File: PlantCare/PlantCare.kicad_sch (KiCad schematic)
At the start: 5 parts, among them U1 AMS1117-3.3

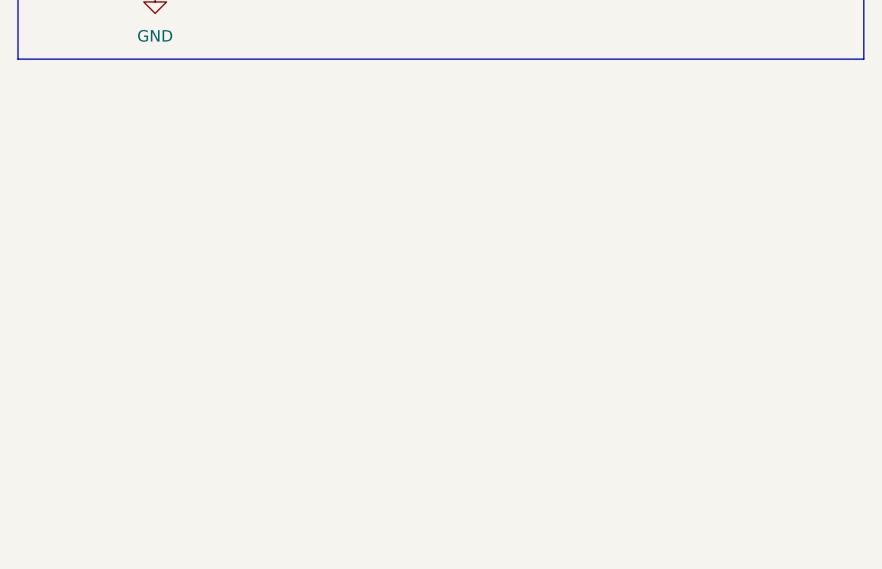
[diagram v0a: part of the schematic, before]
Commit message: Add micro usb scheme
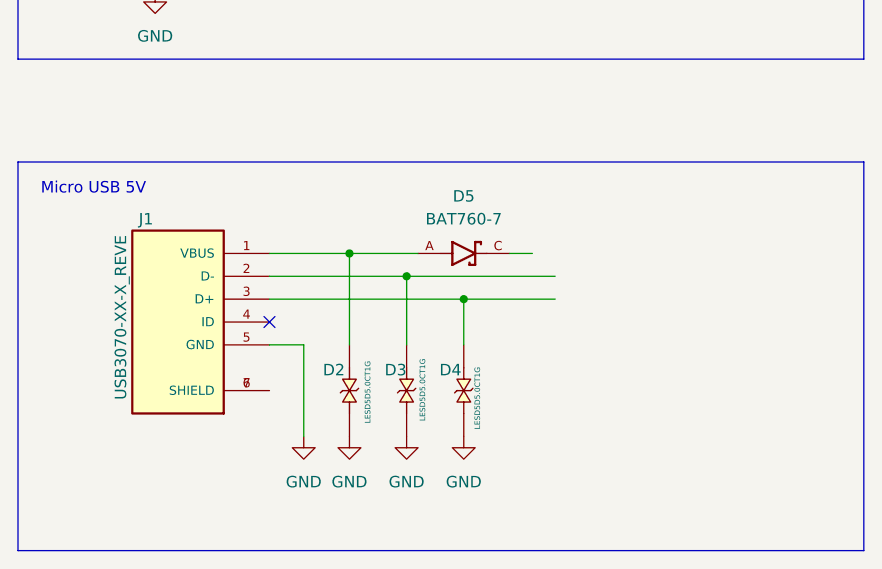
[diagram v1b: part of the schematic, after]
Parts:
- added D2, D3, D4: LESD5D5.0CT1G, TVS_LESD5D5.0CT1G, symbol LESD5D5.0CT1G:LESD5D5.0CT1G
- added D5: BAT760-7, BAT760-7:SOD2513X120N, symbol BAT760-7:BAT760-7
- added J1: USB3070-XX-X_REVE, USB3070-XX-X_REVE:GCT_USB3070-XX-X_REVE, symbol USB3070-XX-X_REVE:USB3070-XX-X_REVE
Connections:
- net GND: now also D2.1, D3.1, D4.2, J1.5 (GND)
- new net: D2.2, D5.A, J1.1 (VBUS)
- new net: D3.2, J1.2 (D-)
- new net: D4.1, J1.3 (D+)
- new net: J1.6 (SHIELD), J1.7 (SHIELD)
- no-connect marks 0 -> 1
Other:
- note added: "Micro USB 5V"

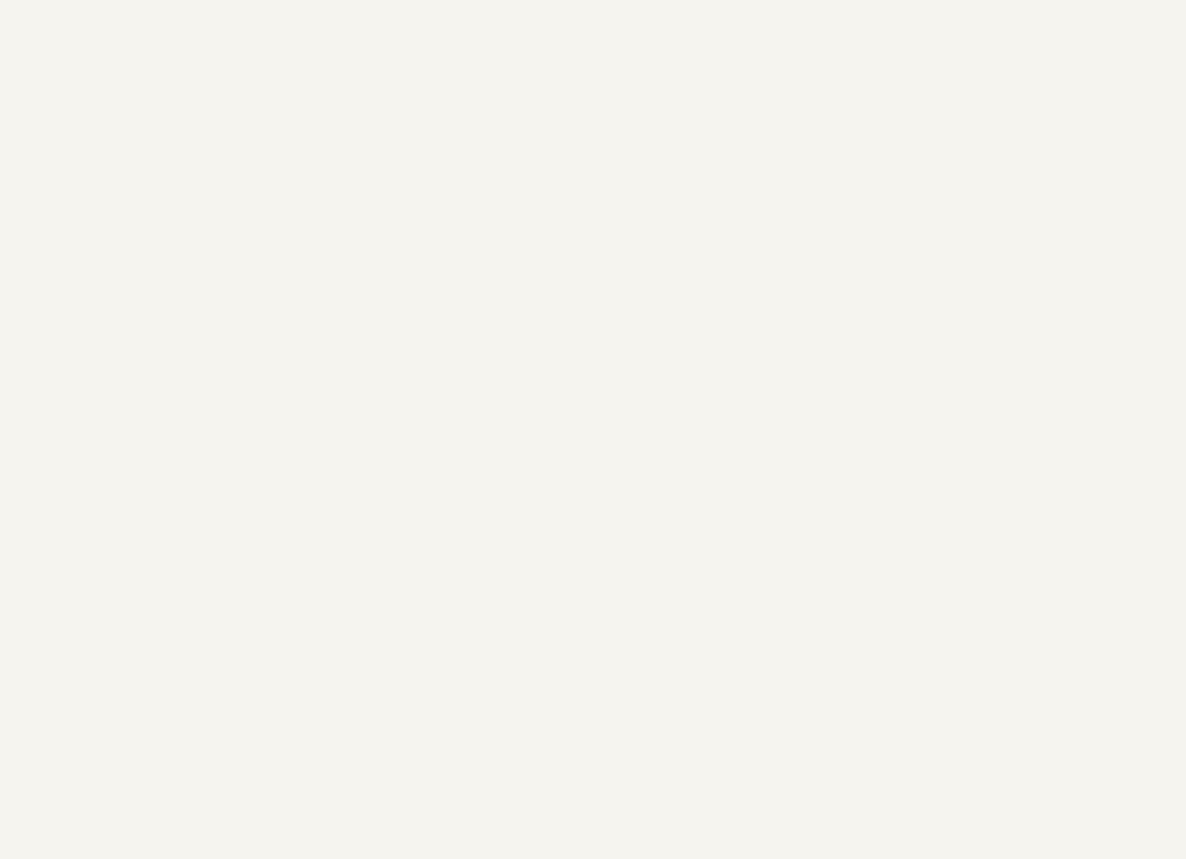
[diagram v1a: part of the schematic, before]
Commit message: Add esp32 module scheme
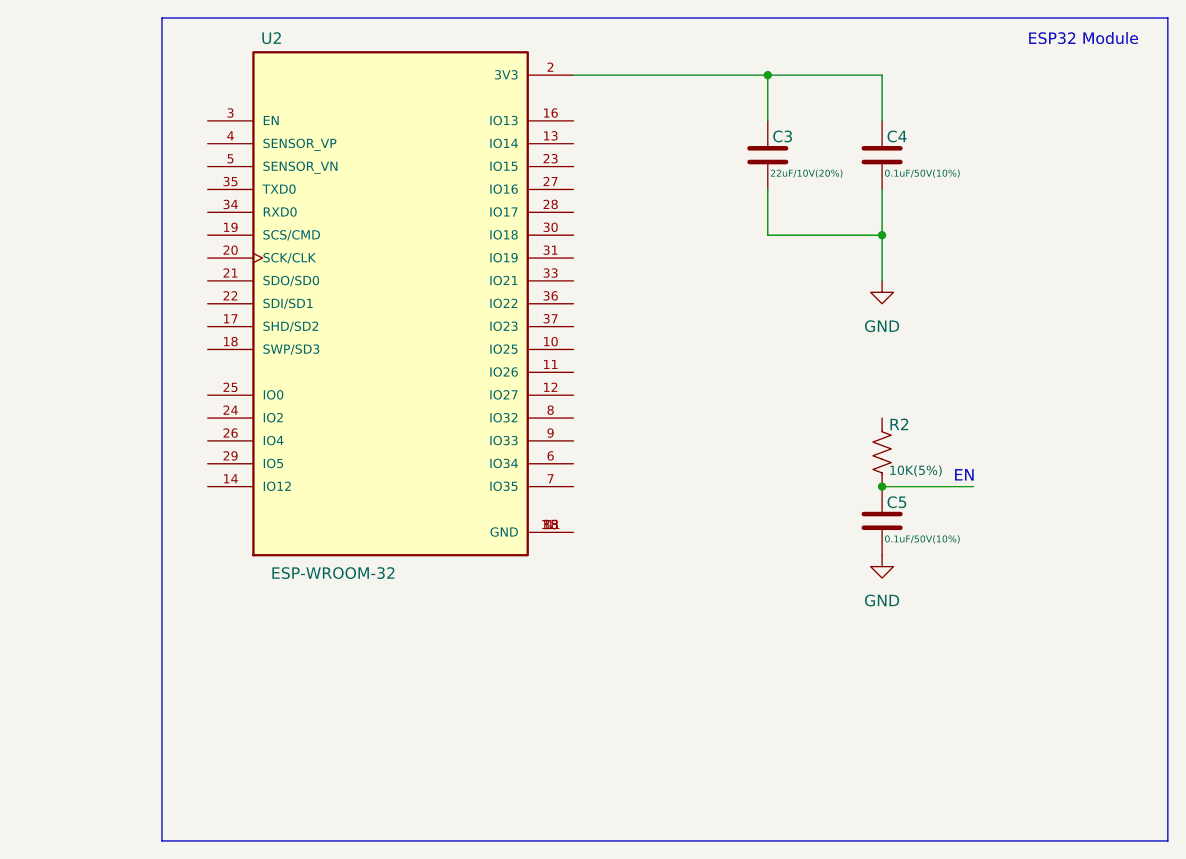
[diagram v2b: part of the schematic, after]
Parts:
- added C3: 22uF/10V(20%), symbol Device:C
- added C4, C5: 0.1uF/50V(10%), symbol Device:C
- added R2: 10K(5%), symbol Device:R_US
- added U2: ESP-WROOM-32, ESP-WROOM-32:MODULE_ESP-WROOM-32, symbol ESP-WROOM-32:ESP-WROOM-32
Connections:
- net GND: now also C3.2, C4.2, C5.2
- new net: C3.1, C4.1, U2.2 (3V3)
- new net: C5.1, R2.2
- new net: U2.1 (GND), U2.1.1 (GND), U2.15 (GND), U2.38 (GND)
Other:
- note added: "EN"
- note added: "ESP32 Module"

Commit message: Prepare schematic
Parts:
- removed C1, C2, C3: 22uF/10V(20%), symbol Device:C
- removed C4, C5: 0.1uF/50V(10%), symbol Device:C
- removed D1: RED LED, symbol Device:LED
- removed D2, D3, D4: LESD5D5.0CT1G, TVS_LESD5D5.0CT1G, symbol LESD5D5.0CT1G:LESD5D5.0CT1G
- removed D5: BAT760-7, BAT760-7:SOD2513X120N, symbol BAT760-7:BAT760-7
- removed J1: USB3070-XX-X_REVE, USB3070-XX-X_REVE:GCT_USB3070-XX-X_REVE, symbol USB3070-XX-X_REVE:USB3070-XX-X_REVE
- removed R1: 2K(5%), symbol Device:R_US
- removed R2: 10K(5%), symbol Device:R_US
- removed U1: AMS1117-3.3, SOT229P700X180-4N, symbol AMS1117-3.3:AMS1117-3.3
- removed U2: ESP-WROOM-32, ESP-WROOM-32:MODULE_ESP-WROOM-32, symbol ESP-WROOM-32:ESP-WROOM-32
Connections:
- no-connect marks 1 -> 0
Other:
- note added: "PLANTCARE MODULE"
- note added: "https://www.espressif.com/sites/default/files/documentation/esp32-wroom-32e_esp32-wroom-32ue_datasheet_en.pdf"
- note removed: "EN"
- note removed: "ESP32 Module"
- note removed: "Micro USB 5V"
- note removed: "POWER SUPPLY"
